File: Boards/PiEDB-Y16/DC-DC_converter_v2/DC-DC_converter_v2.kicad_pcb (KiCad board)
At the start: 2 copper layers, 20 parts

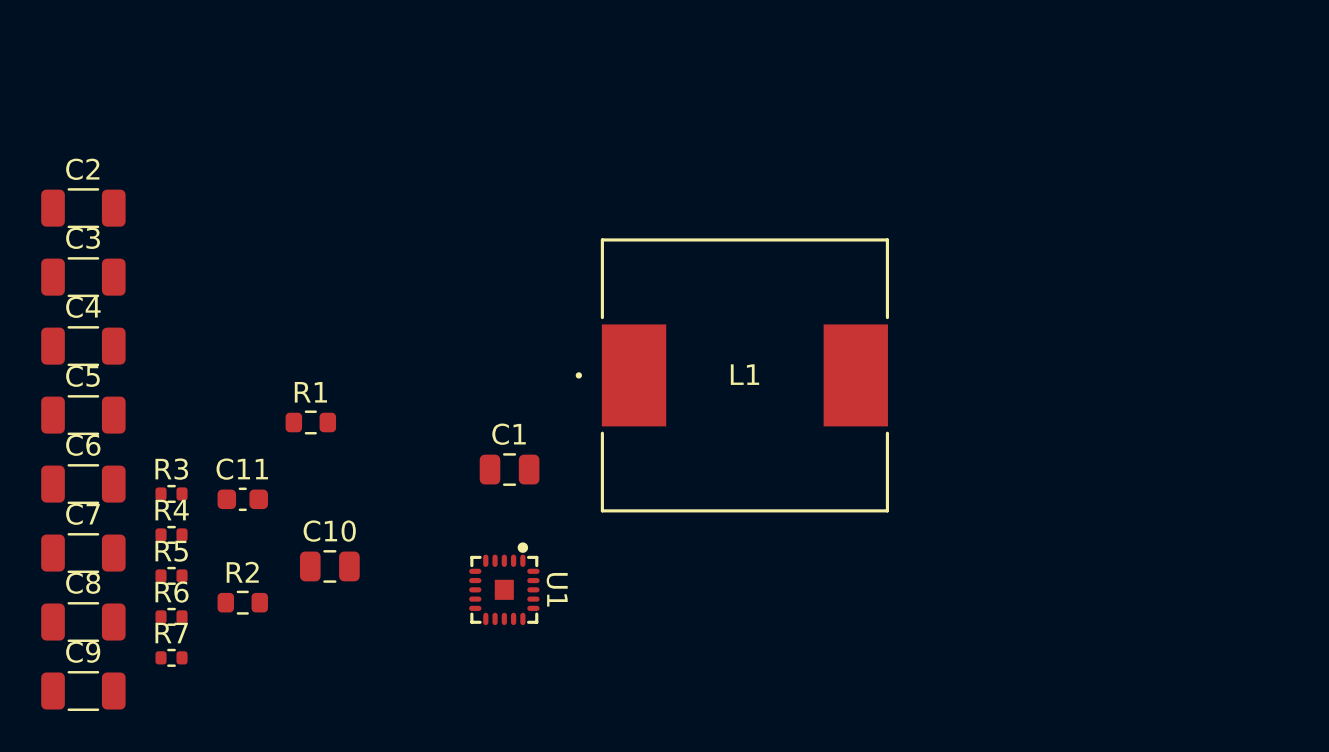
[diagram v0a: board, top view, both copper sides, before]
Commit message: roughly finished layout for new dc-dc converter
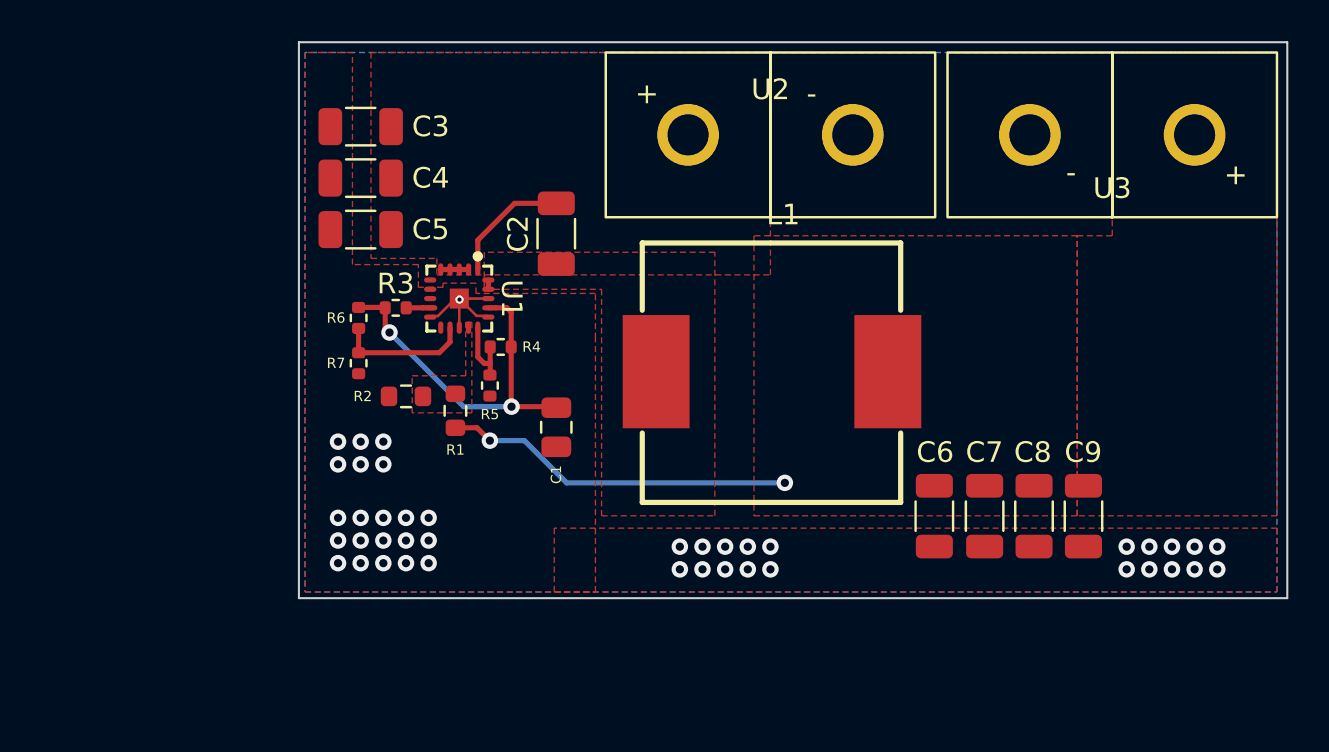
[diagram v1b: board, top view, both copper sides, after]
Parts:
- removed C10: 10n, Capacitor_SMD:C_0805_2012Metric
- removed C11: 100p, Capacitor_SMD:C_0603_1608Metric
- added U2: Anderson_Horizontal, PiE_Footprints:anderson_horizontal, F.Cu at (100.3, 56.2)
- added U3: Anderson_Horizontal, PiE_Footprints:anderson_horizontal, F.Cu at (116.9, 64.2)
- L1: footprint PiE_Footprints:IND_IHLP-5050CE_VIS -> PiE_Footprints:125CDMCCDS-1R8MC
- moved C9 49.3 mm to (115.5, 78.7), turned to 90 degrees
- moved C8 46.5 mm to (113.1, 78.7), turned to 90 degrees
- moved C7 43.8 mm to (110.7, 78.7), turned to 90 degrees
- moved C6 41.4 mm to (108.3, 78.7), turned to 90 degrees
- moved C2 23.0 mm to (89.9, 65.0), turned to 90 degrees
- moved R4 18.4 mm to (87.2, 70.5), turned to 180 degrees
- moved R5 18.0 mm to (86.7, 72.4), turned to -90 degrees
- moved R6 17.1 mm to (80.3, 69.1), turned to -90 degrees
- moved R7 17.0 mm to (80.3, 71.3), turned to -90 degrees
- moved C5 16.2 mm to (80.4, 64.8)
- moved C4 15.7 mm to (80.4, 62.3)
- moved C3 15.3 mm to (80.4, 59.8)
- moved U1 14.3 mm to (85.2, 68.2)
- moved R3 14.2 mm to (82.1, 68.6)
- moved R2 12.8 mm to (82.6, 72.9), turned to 180 degrees
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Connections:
- net Net-(C3-Pad2) renamed /Vin
- net Net-(U1-BST) renamed /BST
- C6 pad 2: Net-(C6-Pad2) -> /Vout
- C7 pad 2: Net-(C6-Pad2) -> /Vout
- C8 pad 2: Net-(C6-Pad2) -> /Vout
- C9 pad 2: Net-(C6-Pad2) -> /Vout
- L1 pad 2: Net-(C6-Pad2) -> /Vout
- R1 pad 1: /SW -> /Vout
- U1 pad 11: Net-(U1-SS) -> unconnected-(U1-SS-Pad11)
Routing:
- net /VCC: track 0.00 -> 18.0 mm, vias 0 -> 2
- net /Vout: track 0.00 -> 17.1 mm, vias 0 -> 2
- net /EN: track 0.00 -> 6.53 mm
- net GND: track 0.00 -> 6.25 mm, vias 0 -> 42
- net /BST: track 0.00 -> 5.98 mm
- net /MODE: track 0.00 -> 3.65 mm
- net Net-(U1-PGOOD): track 0.00 -> 1.39 mm
- net /Vin: track 0.00 -> 1.35 mm
- added copper zone on F.Cu, net /FB
- added copper zone on F.Cu, net /SW
- added copper zone on F.Cu, net /Vin
- added copper zone on F.Cu, net /Vout
- added copper zone on B.Cu, net GND
- added copper zone on F.Cu, net GND
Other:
- board outline added: 48 x 27 mm
- board text added: "Output 5V"

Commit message: updated BOM
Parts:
- R4: value 180k -> 200k
- R6: value 91k -> 100k
- R7: value 55k -> 51k
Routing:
- net /SW: track 0.45 -> 3.61 mm
- net GND: track 6.25 -> 5.98 mm, vias 42 -> 41

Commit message: made contingency board
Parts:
- added J1: 2 Pins, Connector_PinHeader_2.54mm:PinHeader_1x02_P2.54mm_Vertical, F.Cu at (75.3, 68.5)
- C1: value 1u -> 1uF; footprint Capacitor_SMD:C_0805_2012Metric -> Capacitor_SMD:C_0603_1608Metric_Pad1.08x0.95mm_HandSolder
- R7: value 51k -> 15k
- moved C1 9.94 mm to (80.2, 72.0)
- moved R7 6.25 mm to (79.9, 65.0), turned to 180 degrees
- moved R6 4.36 mm to (82.0, 65.0), turned to 180 degrees
- moved C3 2.15 mm to (80.4, 57.6)
- moved C4 2.15 mm to (80.4, 60.1)
- moved C5 2.15 mm to (80.4, 62.6)
- moved C2 2.05 mm to (90.0, 63.0)
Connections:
- C1 pad 1: /VCC -> Net-(U1-SS)
- R6 pad 1: /VCC -> /Vin
- R6 pad 2: /EN -> Net-(J1-Pin_1)
- R7 pad 1: /EN -> Net-(J1-Pin_1)
- U1 pad 11: unconnected-(U1-SS-Pad11) -> Net-(U1-SS)
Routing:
- net Net-(J1-Pin_1): track 0.00 -> 8.28 mm, vias 0 -> 2
- net /SW: track 3.61 -> 8.96 mm, vias 0 -> 2
- net Net-(U1-SS): track 0.00 -> 4.69 mm
- net /EN: track 6.53 -> 10.3 mm, vias 0 -> 1
- net /VCC: track 18.0 -> 21.0 mm
- net /BST: track 5.98 -> 6.74 mm
- net GND: vias 41 -> 47
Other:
- board size 48 x 27 mm -> 53.2 x 27 mm
- board text added: "Built-In EN"
